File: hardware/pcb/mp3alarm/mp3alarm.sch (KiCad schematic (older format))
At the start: 14 parts, among them J1 AUDIO, J2 SW0, J3 SW1, J4 SW2, J5 I2C, J6 TM1637, J7 microSD, J9 ANT, U1 UDA1334A_Breakout, U2 mini_esp32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

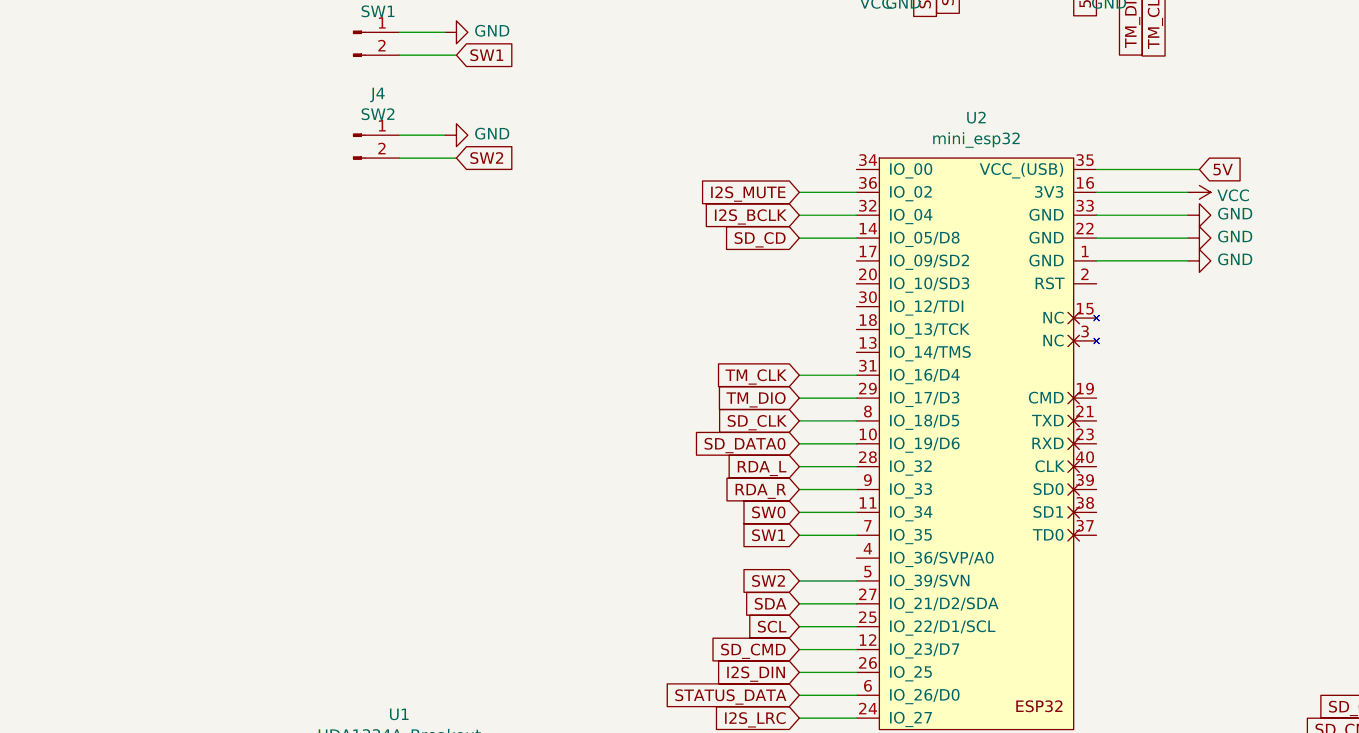
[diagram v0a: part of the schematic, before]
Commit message: Updated PCB (added QR code, OSHW logo, etc) Some bugfixes for webinterface Updated README
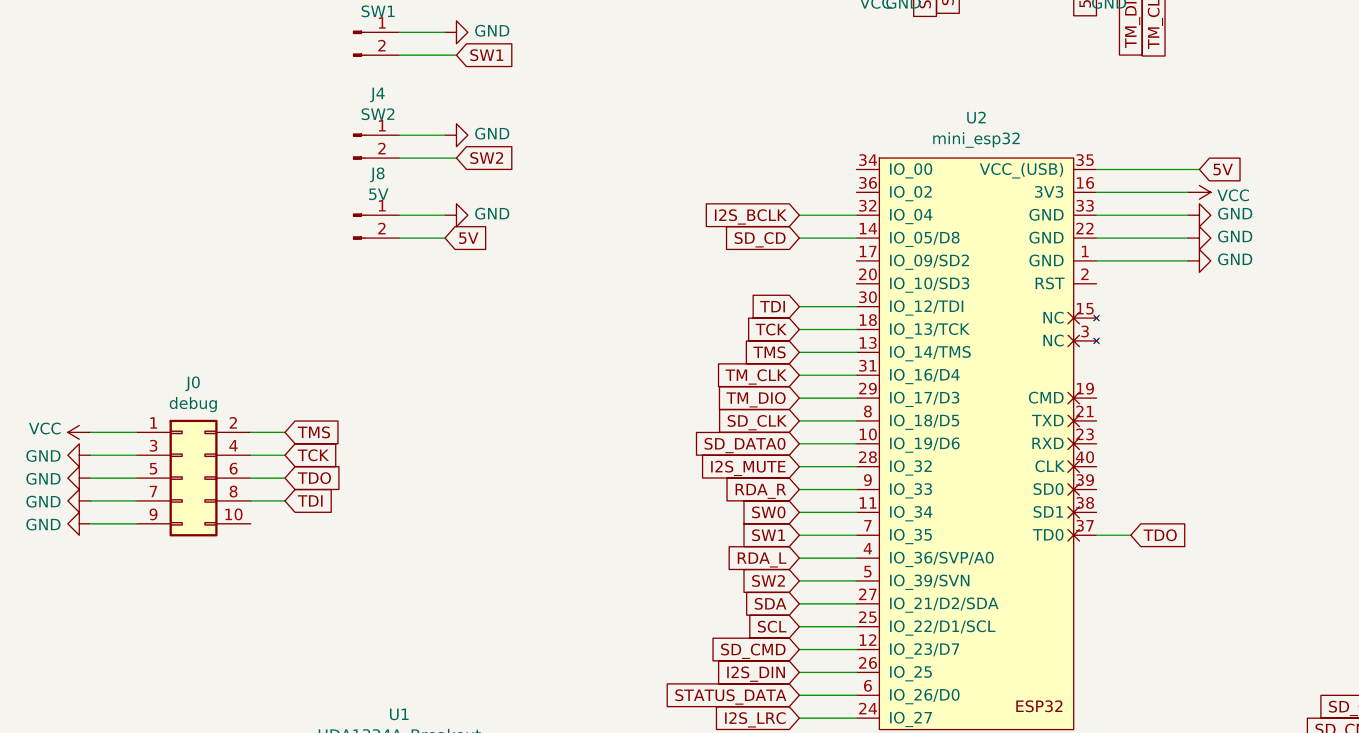
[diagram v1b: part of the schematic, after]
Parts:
- added J0: debug, Connector_PinHeader_2.54mm:PinHeader_2x05_P2.54mm_Vertical_SMD, symbol Connector_Generic:Conn_02x05_Odd_Even
- added J8: 5V, Connector_PinHeader_2.54mm:PinHeader_1x02_P2.54mm_Vertical, symbol Connector:Conn_01x02_Male
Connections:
- net 5V: now also J8.2 (Pin_2)
- net GND: now also J0.3 (Pin_3), J0.5 (Pin_5), J0.7 (Pin_7), J0.9 (Pin_9), J8.1 (Pin_1)
- net I2S_MUTE: now also U2.28 (IO_32); no longer U2.36 (IO_02)
- net RDA_L: now also U2.4 (IO_36/SVP/A0); no longer U2.28 (IO_32)
- net VCC: now also J0.1 (Pin_1)
- net TMS: now reaches U2.13 (IO_14/TMS)
- net TMS: now also J0.2 (Pin_2)
- net TCK: now reaches U2.18 (IO_13/TCK)
- net TCK: now also J0.4 (Pin_4)
- net TDI: now reaches U2.30 (IO_12/TDI)
- net TDI: now also J0.8 (Pin_8)
- net TDO: now reaches U2.37 (TD0)
- net TDO: now also J0.6 (Pin_6)
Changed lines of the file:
@@
 Wire Wire Line
 	3650 5550 3450 5550
-Text GLabel 4750 4000 0    50   Input ~ 0
+Text GLabel 4750 4400 0    50   Input ~ 0
 RDA_L
 Text GLabel 4750 4100 0    50   Input ~ 0
 RDA_R
-Wire Wire Line
-	4750 4000 5000 4000
 Wire Wire Line
 	4750 4100 5000 4100
@@
 Text GLabel 4750 4300 0    50   Input ~ 0
 SW1
-Text GLabel 4750 2800 0    50   Input ~ 0
+Text GLabel 4750 4000 0    50   Input ~ 0
 I2S_MUTE
 Wire Wire Line
@@
 Wire Wire Line
 	5000 4200 4750 4200
-Wire Wire Line
-	4750 2800 5000 2800
 $Comp
 L power:GND #PWR02
@@
 Wire Wire Line
 	4750 5000 5000 5000
+Wire Wire Line
+	4750 4400 5000 4400
+Wire Wire Line
+	4750 4000 5000 4000
+$Comp
+L Connector:Conn_01x02_Male J8
+U 1 1 5FFA7191
+P 2800 2900
+F 0 "J8" H 2908 3081 50  0000 C CNN
+F 1 "5V" H 2908 2990 50  0000 C CNN
+F 2 "Connector_PinHeader_2.54mm:PinHeader_1x02_P2.54mm_Vertical" H 2800 2900 50  0001 C CNN
+F 3 "~" H 2800 2900 50  0001 C CNN
+	1    2800 2900
+	1    0    0    -1
+$EndComp
+$Comp
+L power:GND #PWR0101
+U 1 1 5FFA77AD
+P 3200 2900
+F 0 "#PWR0101" H 3200 2650 50  0001 C CNN
+F 1 "GND" V 3205 2772 50  0000 R CNN
+F 2 "" H 3200 2900 50  0001 C CNN
+F 3 "" H 3200 2900 50  0001 C CNN
+	1    3200 2900
+	0    -1   -1   0
+$EndComp
+Text GLabel 3200 3000 2    50   Input ~ 0
+5V
+Wire Wire Line
+	3200 3000 3000 3000
+Wire Wire Line
+	3200 2900 3000 2900
+Text GLabel 2500 3850 2    50   Input ~ 0
+TMS
+Text GLabel 2500 4050 2    50   Input ~ 0
+TDO
+Text GLabel 2500 4150 2    50   Input ~ 0
+TDI
+Text GLabel 2500 3950 2    50   Input ~ 0
+TCK
+$Comp
+L Connector_Generic:Conn_02x05_Odd_Even J0
+U 1 1 5FFCFAB1
+P 2050 4050
+F 0 "J0" H 2100 4467 50  0000 C CNN
+F 1 "debug" H 2100 4376 50  0000 C CNN
+F 2 "Connector_PinHeader_2.54mm:PinHeader_2x05_P2.54mm_Vertical_SMD" H 2050 4050 50  0001 C CNN
+F 3 "~" H 2050 4050 50  0001 C CNN
+	1    2050 4050
+	1    0    0    -1
+$EndComp
+$Comp
+L power:VCC #PWR0102
+U 1 1 5FFD0F20
+P 1650 3850
+F 0 "#PWR0102" H 1650 3700 50  0001 C CNN
+F 1 "VCC" V 1665 3978 50  0000 L CNN
+F 2 "" H 1650 3850 50  0001 C CNN
+F 3 "" H 1650 3850 50  0001 C CNN
+	1    1650 3850
+	0    -1   -1   0
+$EndComp
+$Comp
+L power:GND #PWR0103
+U 1 1 5FFD5D90
+P 1650 3950
+F 0 "#PWR0103" H 1650 3700 50  0001 C CNN
+F 1 "GND" V 1655 3822 50  0000 R CNN
+F 2 "" H 1650 3950 50  0001 C CNN
+F 3 "" H 1650 3950 50  0001 C CNN
+	1    1650 3950
+	0    1    1    0
+$EndComp
+$Comp
+L power:GND #PWR0104
+U 1 1 5FFD6265
+P 1650 4050
+F 0 "#PWR0104" H 1650 3800 50  0001 C CNN
+F 1 "GND" V 1655 3922 50  0000 R CNN
+F 2 "" H 1650 4050 50  0001 C CNN
+F 3 "" H 1650 4050 50  0001 C CNN
+	1    1650 4050
+	0    1    1    0
+$EndComp
+$Comp
+L power:GND #PWR0105
+U 1 1 5FFD6381
+P 1650 4150
+F 0 "#PWR0105" H 1650 3900 50  0001 C CNN
+F 1 "GND" V 1655 4022 50  0000 R CNN
+F 2 "" H 1650 4150 50  0001 C CNN
+F 3 "" H 1650 4150 50  0001 C CNN
+	1    1650 4150
+	0    1    1    0
+$EndComp
+$Comp
+L power:GND #PWR0106
+U 1 1 5FFD658B
+P 1650 4250
+F 0 "#PWR0106" H 1650 4000 50  0001 C CNN
+F 1 "GND" V 1655 4122 50  0000 R CNN
+F 2 "" H 1650 4250 50  0001 C CNN
+F 3 "" H 1650 4250 50  0001 C CNN
+	1    1650 4250
+	0    1    1    0
+$EndComp
+Wire Wire Line
+	2500 3850 2350 3850
+Wire Wire Line
+	2500 3950 2350 3950
+Wire Wire Line
+	2350 4050 2500 4050
+Wire Wire Line
+	2500 4150 2350 4150
+Wire Wire Line
+	1850 4250 1650 4250
+Wire Wire Line
+	1650 4150 1850 4150
+Wire Wire Line
+	1850 4050 1650 4050
+Wire Wire Line
+	1650 3950 1850 3950
+Wire Wire Line
+	1850 3850 1650 3850
+Text GLabel 4750 3500 0    50   Input ~ 0
+TMS
+Text GLabel 4750 3400 0    50   Input ~ 0
+TCK
+Text GLabel 6200 4300 2    50   Input ~ 0
+TDO
+Text GLabel 4750 3300 0    50   Input ~ 0
+TDI
+Wire Wire Line
+	4750 3300 5000 3300
+Wire Wire Line
+	4750 3400 5000 3400
+Wire Wire Line
+	4750 3500 5000 3500
+Wire Wire Line
+	6200 4300 6050 4300
 $EndSCHEMATC
